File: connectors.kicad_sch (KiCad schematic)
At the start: 4 parts, among them J1 Conn_01x04_Pin, J2 Conn_01x04_Pin, J3 Conn_01x09_Pin, J4 Conn_02x03_Odd_Even

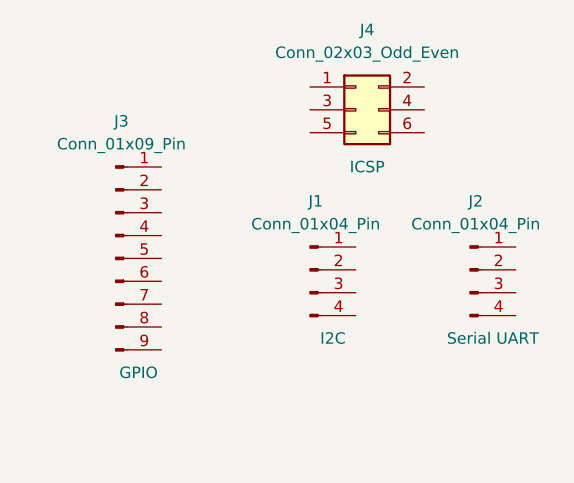
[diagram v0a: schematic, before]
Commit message: changed symbol locations (arranged)
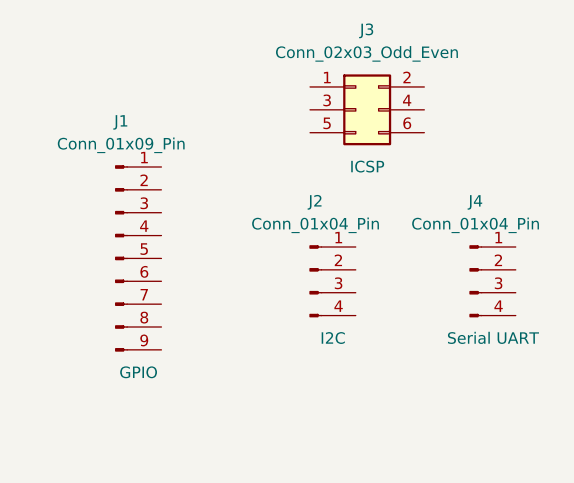
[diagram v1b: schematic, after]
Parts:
- renumbered J3 to J1, J1 to J2, J4 to J3, J2 to J4
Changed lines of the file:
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@@
 		(in_pos_files yes)
 		(dnp no)
-		(property "Reference" "J4"
+		(property "Reference" "J3"
 			(at 87.63 36.83 0)
 			(show_name no)
@@
 			(project "MCU Datalogger"
 				(path "/046ed9df-8a70-4e0e-95d6-1fb540a15377/37d5f673-6493-4ca5-aec1-606f4a707970"
-					(reference "J4")
+					(reference "J3")
 					(unit 1)
 				)
@@
 		(in_pos_files yes)
 		(dnp no)
-		(property "Reference" "J3"
+		(property "Reference" "J1"
 			(at 60.325 46.99 0)
 			(show_name no)
@@
 			(project "MCU Datalogger"
 				(path "/046ed9df-8a70-4e0e-95d6-1fb540a15377/37d5f673-6493-4ca5-aec1-606f4a707970"
-					(reference "J3")
+					(reference "J1")
 					(unit 1)
 				)
@@
 		(in_pos_files yes)
 		(dnp no)
-		(property "Reference" "J1"
+		(property "Reference" "J2"
 			(at 81.915 55.88 0)
 			(show_name no)
@@
 			(project "MCU Datalogger"
 				(path "/046ed9df-8a70-4e0e-95d6-1fb540a15377/37d5f673-6493-4ca5-aec1-606f4a707970"
-					(reference "J1")
+					(reference "J2")
 					(unit 1)
 				)
@@
 		(in_pos_files yes)
 		(dnp no)
-		(property "Reference" "J2"
+		(property "Reference" "J4"
 			(at 99.695 55.88 0)
 			(show_name no)
@@
 			(project "MCU Datalogger"
 				(path "/046ed9df-8a70-4e0e-95d6-1fb540a15377/37d5f673-6493-4ca5-aec1-606f4a707970"
-					(reference "J2")
+					(reference "J4")
 					(unit 1)
 				)

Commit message: alloted footprints and completed wiring of main sheet
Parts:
- J1: footprint (none) -> Connector_PinHeader_2.54mm:PinHeader_1x09_P2.54mm_Vertical
- J2, J4: footprint (none) -> Connector_PinHeader_2.54mm:PinHeader_1x04_P2.54mm_Vertical
- J3: footprint (none) -> Connector_PinHeader_2.54mm:PinHeader_2x03_P2.54mm_Vertical
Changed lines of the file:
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@@
 			)
 		)
-		(property "Footprint" ""
+		(property "Footprint" "Connector_PinHeader_2.54mm:PinHeader_2x03_P2.54mm_Vertical"
 			(at 86.36 45.72 0)
 			(hide yes)
@@
 			)
 		)
-		(property "Footprint" ""
+		(property "Footprint" "Connector_PinHeader_2.54mm:PinHeader_1x09_P2.54mm_Vertical"
 			(at 59.69 62.23 0)
 			(hide yes)
@@
 			)
 		)
-		(property "Footprint" ""
+		(property "Footprint" "Connector_PinHeader_2.54mm:PinHeader_1x04_P2.54mm_Vertical"
 			(at 81.28 63.5 0)
 			(hide yes)
@@
 			)
 		)
-		(property "Footprint" ""
+		(property "Footprint" "Connector_PinHeader_2.54mm:PinHeader_1x04_P2.54mm_Vertical"
 			(at 99.06 63.5 0)
 			(hide yes)

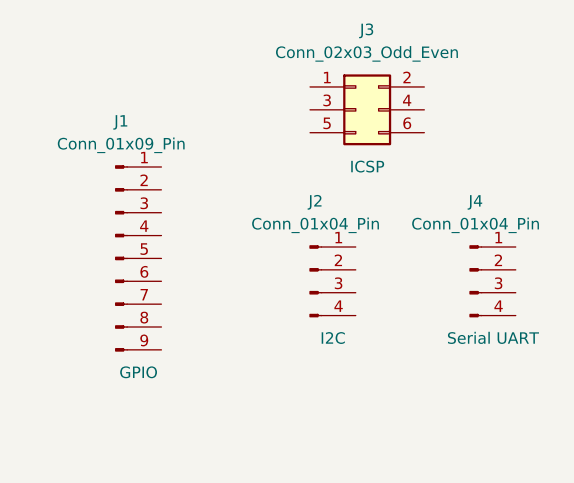
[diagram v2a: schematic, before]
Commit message: completed the wiring of sheet 2 and allocated power net class to GND and VCC
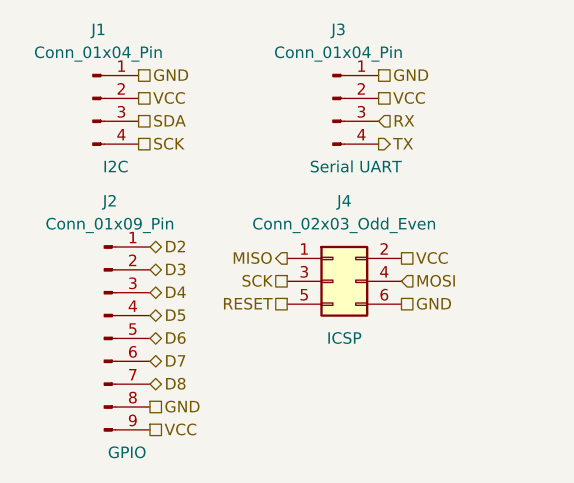
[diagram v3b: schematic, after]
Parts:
- J1: renamed from J4; Purpose Serial UART -> I2C
- J3: renamed from J2; Purpose I2C -> Serial UART
- renumbered J1 to J2, J3 to J4
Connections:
- net MISO: now reaches J4.1 (Pin_1)
- net VCC: now reaches J4.2 (Pin_2)
- net VCC: now also J1.2 (Pin_2), J2.9 (Pin_9), J3.2 (Pin_2)
- net SCK: now reaches J4.3 (Pin_3)
- net SCK: now also J1.4 (Pin_4)
- net MOSI: now reaches J4.4 (Pin_4)
- net RESET: now reaches J4.5 (Pin_5)
- net GND: now reaches J4.6 (Pin_6)
- net GND: now also J1.1 (Pin_1), J2.8 (Pin_8), J3.1 (Pin_1)
- net D2: now reaches J2.1 (Pin_1)
- net D3: now reaches J2.2 (Pin_2)
- net D4: now reaches J2.3 (Pin_3)
- net D5: now reaches J2.4 (Pin_4)
- net D6: now reaches J2.5 (Pin_5)
- net D7: now reaches J2.6 (Pin_6)
- net D8: now reaches J2.7 (Pin_7)
- net RX: now reaches J3.3 (Pin_3)
- net TX: now reaches J3.4 (Pin_4)
- net SDA: now reaches J1.3 (Pin_3)
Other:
- moved on the sheet: J1, J2, J3, J4
